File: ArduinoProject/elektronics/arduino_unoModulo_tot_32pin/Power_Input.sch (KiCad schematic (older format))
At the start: 8 parts, among them IC401 MC33269ST-5.OT3, U401 battery, U402 LP2985-3.3

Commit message: sensormodule_x4 added
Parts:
- removed U401: battery, symbol battery
- added X2: DG3XX-02-3.5, degson_DG350-3.5-02P, symbol DG3XX-02-3.5
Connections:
- wire segments 22 -> 20
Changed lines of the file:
@@
 LIBS:MFN_Atmel
 LIBS:MFN_STMicro
+LIBS:degson
 LIBS:Arduino_Uno_R3_From_Scratch-cache
 EELAYER 25 0
@@
 $EndComp
 $Comp
-L battery U401
-U 1 1 5A970BE8
-P 3050 2700
-F 0 "U401" H 3350 1650 60  0000 C CNN
-F 1 "battery" H 2700 2950 60  0000 C CNN
-F 2 "" H 2700 2600 60  0001 C CNN
-F 3 "" H 2700 2600 60  0001 C CNN
-	1    3050 2700
-	1    0    0    -1
-$EndComp
-$Comp
 L D D401
 U 1 1 5A970C82
@@
 Wire Wire Line
 	4450 2800 4850 2800
-Wire Wire Line
-	3000 2300 3900 2300
-Wire Wire Line
-	3900 2300 3900 3900
 $Comp
 L GND #PWR015
 U 1 1 5A970D05
-P 3900 3900
-F 0 "#PWR015" H 3900 3650 50  0001 C CNN
-F 1 "GND" H 3900 3750 50  0000 C CNN
-F 2 "" H 3900 3900 50  0001 C CNN
-F 3 "" H 3900 3900 50  0001 C CNN
-	1    3900 3900
-	1    0    0    -1
-$EndComp
-Wire Wire Line
-	3650 3450 3900 3450
-Connection ~ 3900 3450
+P 3850 2950
+F 0 "#PWR015" H 3850 2700 50  0001 C CNN
+F 1 "GND" H 3850 2800 50  0000 C CNN
+F 2 "" H 3850 2950 50  0001 C CNN
+F 3 "" H 3850 2950 50  0001 C CNN
+	1    3850 2950
+	1    0    0    -1
+$EndComp
 Wire Wire Line
 	4050 2800 4050 2900
@@
 Wire Wire Line
 	7050 2800 5850 2800
-Wire Wire Line
-	6050 2550 6050 3600
 Connection ~ 6050 2800
 Wire Wire Line
@@
 	1    0    0    -1
 $EndComp
+Wire Wire Line
+	6050 2550 6050 3600
+Connection ~ 6050 2900
+Wire Wire Line
+	3650 2950 3850 2950
+$Comp
+L DG3XX-02-3.5 X2
+U 1 1 5AA016CD
+P 3550 2800
+F 0 "X2" H 3670 2765 45  0000 L BNN
+F 1 "DG3XX-02-3.5" H 3550 2800 45  0001 L BNN
+F 2 "degson_DG350-3.5-02P" H 3580 2950 20  0001 C CNN
+F 3 "" H 3550 2800 60  0001 C CNN
+	1    3550 2800
+	-1   0    0    1
+$EndComp
+$Comp
+L DG3XX-02-3.5 X2
+U 2 1 5AA0177C
+P 3550 2950
+F 0 "X2" H 3670 2915 45  0000 L BNN
+F 1 "DG3XX-02-3.5" H 3550 2950 45  0001 L BNN
+F 2 "degson_DG350-3.5-02P" H 3580 3100 20  0001 C CNN
+F 3 "" H 3550 2950 60  0001 C CNN
+	2    3550 2950
+	-1   0    0    1
+$EndComp
 $EndSCHEMATC

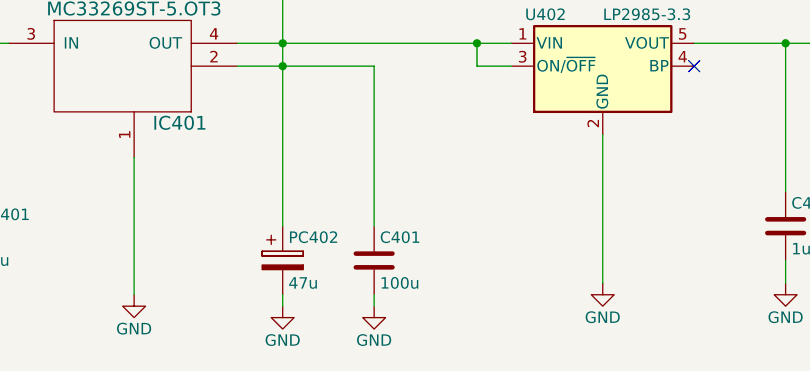
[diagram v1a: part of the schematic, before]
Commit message: arduino routed
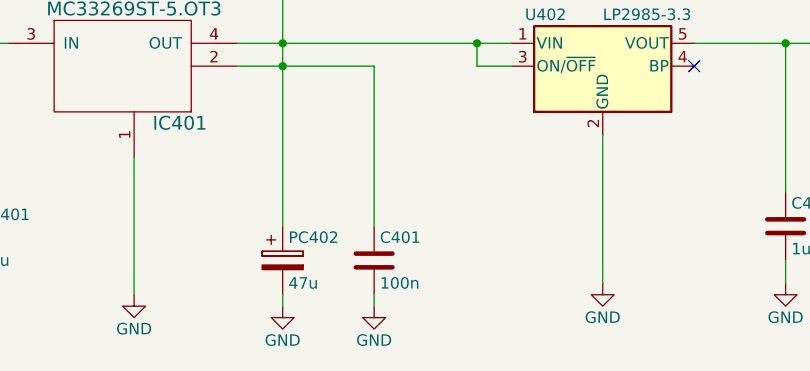
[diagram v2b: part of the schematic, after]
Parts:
- C401: value 100u -> 100n
- IC401: footprint (none) -> MC33269ST-3.3T3G:SOT230P700X175-4N
- X2: footprint degson_DG350-3.5-02P -> degson:degson-DG350-3.5-02P
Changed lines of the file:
@@
 F 0 "IC401" H 5600 2650 60  0000 C CNN
 F 1 "MC33269ST-5.OT3" H 5400 3150 60  0000 C CNN
-F 2 "" H 5050 2800 60  0001 C CNN
+F 2 "MC33269ST-3.3T3G:SOT230P700X175-4N" H 5050 2800 60  0001 C CNN
 F 3 "" H 5050 2800 60  0001 C CNN
 	1    5400 2900
@@
 P 6450 3750
 F 0 "C401" H 6475 3850 50  0000 L CNN
-F 1 "100u" H 6475 3650 50  0000 L CNN
+F 1 "100n" H 6475 3650 50  0000 L CNN
 F 2 "Capacitors_SMD:C_0805" H 6488 3600 50  0001 C CNN
 F 3 "" H 6450 3750 50  0001 C CNN
@@
 F 0 "X2" H 3670 2765 45  0000 L BNN
 F 1 "DG3XX-02-3.5" H 3550 2800 45  0001 L BNN
-F 2 "degson_DG350-3.5-02P" H 3580 2950 20  0001 C CNN
+F 2 "degson:degson-DG350-3.5-02P" H 3580 2950 20  0001 C CNN
 F 3 "" H 3550 2800 60  0001 C CNN
 	1    3550 2800
@@
 F 0 "X2" H 3670 2915 45  0000 L BNN
 F 1 "DG3XX-02-3.5" H 3550 2950 45  0001 L BNN
-F 2 "degson_DG350-3.5-02P" H 3580 3100 20  0001 C CNN
+F 2 "degson:degson-DG350-3.5-02P" H 3580 3100 20  0001 C CNN
 F 3 "" H 3550 2950 60  0001 C CNN
 	2    3550 2950

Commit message: new components2
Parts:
- removed U402: LP2985-3.3, TO_SOT_Packages_SMD:SOT-23-5, symbol LP2985-3.3
- added IC402: MC33269ST-5.OT3, PHT6NQ10T_135:SOT230P700X180-4N, symbol MC33269ST-5.OT3
- D401: footprint Diodes_SMD:D_0805 -> Diodes_SMD:D_MicroMELF_Hadsoldering
- IC401: footprint MC33269ST-3.3T3G:SOT230P700X175-4N -> PHT6NQ10T_135:SOT230P700X180-4N
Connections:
- net +3V3: now also IC402.2, IC402.4 (OUT)
- net +5V: now also IC402.3 (IN)
- net GND: now also IC402.1
- no-connect marks 1 -> 0
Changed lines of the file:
@@
 $EndDescr
-$Comp
-L LP2985-3.3 U402
-U 1 1 5A9664D2
-P 7450 2900
-F 0 "U402" H 7200 3125 50  0000 C CNN
-F 1 "LP2985-3.3" H 7450 3125 50  0000 L CNN
-F 2 "TO_SOT_Packages_SMD:SOT-23-5" H 7450 3225 50  0001 C CNN
-F 3 "" H 7450 2900 50  0001 C CNN
-	1    7450 2900
-	1    0    0    -1
-$EndComp
 $Comp
 L MC33269ST-5.OT3 IC401
@@
 F 0 "IC401" H 5600 2650 60  0000 C CNN
 F 1 "MC33269ST-5.OT3" H 5400 3150 60  0000 C CNN
-F 2 "MC33269ST-3.3T3G:SOT230P700X175-4N" H 5050 2800 60  0001 C CNN
+F 2 "PHT6NQ10T_135:SOT230P700X180-4N" H 5050 2800 60  0001 C CNN
 F 3 "" H 5050 2800 60  0001 C CNN
 	1    5400 2900
@@
 F 0 "D401" H 4300 2900 50  0000 C CNN
 F 1 "D" H 4300 2700 50  0000 C CNN
-F 2 "Diodes_SMD:D_0805" H 4300 2800 50  0001 C CNN
+F 2 "Diodes_SMD:D_MicroMELF_Hadsoldering" H 4300 2800 50  0001 C CNN
 F 3 "" H 4300 2800 50  0001 C CNN
 	1    4300 2800
@@
 Wire Wire Line
 	5400 3900 5400 3300
-Wire Wire Line
-	7050 2800 5850 2800
 Connection ~ 6050 2800
 Wire Wire Line
-	7050 2900 6900 2900
-Wire Wire Line
-	6900 2900 6900 2800
-Connection ~ 6900 2800
-Wire Wire Line
-	7850 2800 8400 2800
+	7700 2800 8400 2800
 Wire Wire Line
 	8250 2800 8250 3450
@@
 L GND #PWR019
 U 1 1 5A97100A
-P 7450 3850
-F 0 "#PWR019" H 7450 3600 50  0001 C CNN
-F 1 "GND" H 7450 3700 50  0000 C CNN
-F 2 "" H 7450 3850 50  0001 C CNN
-F 3 "" H 7450 3850 50  0001 C CNN
-	1    7450 3850
-	1    0    0    -1
-$EndComp
-Wire Wire Line
-	7450 3850 7450 3200
+P 7250 3950
+F 0 "#PWR019" H 7250 3700 50  0001 C CNN
+F 1 "GND" H 7250 3800 50  0000 C CNN
+F 2 "" H 7250 3950 50  0001 C CNN
+F 3 "" H 7250 3950 50  0001 C CNN
+	1    7250 3950
+	1    0    0    -1
+$EndComp
+Wire Wire Line
+	7250 3950 7250 3300
 Wire Wire Line
 	5850 2900 6450 2900
@@
 Wire Wire Line
 	6050 3950 6050 3900
-NoConn ~ 7850 2900
 Connection ~ 8250 2800
 Text HLabel 8400 2800 2    60   Input ~ 0
@@
 	-1   0    0    1
 $EndComp
+$Comp
+L MC33269ST-5.OT3 IC402
+U 1 1 5AA92A2E
+P 7250 2900
+F 0 "IC402" H 7450 2650 60  0000 C CNN
+F 1 "MC33269ST-5.OT3" H 7250 3150 60  0000 C CNN
+F 2 "PHT6NQ10T_135:SOT230P700X180-4N" H 6900 2800 60  0001 C CNN
+F 3 "" H 6900 2800 60  0001 C CNN
+	1    7250 2900
+	1    0    0    -1
+$EndComp
+Wire Wire Line
+	5850 2800 6700 2800
+Wire Wire Line
+	7700 2900 7825 2900
+Wire Wire Line
+	7825 2900 7825 2800
+Connection ~ 7825 2800
 $EndSCHEMATC

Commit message: changes made
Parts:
- D401: footprint Diodes_SMD:D_MicroMELF_Hadsoldering -> Diodes_SMD:D_MiniMELF_Handsoldering
- PC401, PC402: footprint Capacitors_SMD:CP_Elec_4x5.3 -> Capacitors_SMD:CP_Elec_6.3x5.3
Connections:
- net +5V: now also C401.2; no longer C401.1
- net GND: now also C401.1; no longer C401.2
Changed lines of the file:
@@
 F 0 "D401" H 4300 2900 50  0000 C CNN
 F 1 "D" H 4300 2700 50  0000 C CNN
-F 2 "Diodes_SMD:D_MicroMELF_Hadsoldering" H 4300 2800 50  0001 C CNN
+F 2 "Diodes_SMD:D_MiniMELF_Handsoldering" H 4300 2800 50  0001 C CNN
 F 3 "" H 4300 2800 50  0001 C CNN
 	1    4300 2800
 	-1   0    0    1
 $EndComp
-Wire Wire Line
-	3650 2800 4150 2800
-Wire Wire Line
-	4450 2800 4850 2800
 $Comp
 L GND #PWR015
@@
 	1    0    0    -1
 $EndComp
-Wire Wire Line
-	4050 2800 4050 2900
-Connection ~ 4050 2800
 Text HLabel 4050 2900 3    60   Input ~ 0
 PWRIN
-Wire Wire Line
-	4500 2800 4500 2650
-Connection ~ 4500 2800
 Text HLabel 4500 2650 1    60   Input ~ 0
 VIN
-Wire Wire Line
-	4700 2800 4700 3500
-Connection ~ 4700 2800
 $Comp
 L CP PC401
@@
 F 0 "PC401" H 4725 3750 50  0000 L CNN
 F 1 "47u" H 4725 3550 50  0000 L CNN
-F 2 "Capacitors_SMD:CP_Elec_4x5.3" H 4738 3500 50  0001 C CNN
+F 2 "Capacitors_SMD:CP_Elec_6.3x5.3" H 4738 3500 50  0001 C CNN
 F 3 "" H 4700 3650 50  0001 C CNN
 	1    4700 3650
@@
 	1    0    0    -1
 $EndComp
-Wire Wire Line
-	4700 3900 4700 3800
-$Comp
-L GND #PWR017
-U 1 1 5A970E5B
-P 5400 3900
-F 0 "#PWR017" H 5400 3650 50  0001 C CNN
-F 1 "GND" H 5400 3750 50  0000 C CNN
-F 2 "" H 5400 3900 50  0001 C CNN
-F 3 "" H 5400 3900 50  0001 C CNN
-	1    5400 3900
-	1    0    0    -1
-$EndComp
-Wire Wire Line
-	5400 3900 5400 3300
-Connection ~ 6050 2800
-Wire Wire Line
-	7700 2800 8400 2800
-Wire Wire Line
-	8250 2800 8250 3450
 $Comp
 L C C402
@@
 $EndComp
 $Comp
-L GND #PWR018
+L GND #PWR017
 U 1 1 5A970FC8
 P 8250 3850
-F 0 "#PWR018" H 8250 3600 50  0001 C CNN
+F 0 "#PWR017" H 8250 3600 50  0001 C CNN
 F 1 "GND" H 8250 3700 50  0000 C CNN
 F 2 "" H 8250 3850 50  0001 C CNN
@@
 	1    0    0    -1
 $EndComp
-Wire Wire Line
-	8250 3850 8250 3750
-$Comp
-L GND #PWR019
-U 1 1 5A97100A
-P 7250 3950
-F 0 "#PWR019" H 7250 3700 50  0001 C CNN
-F 1 "GND" H 7250 3800 50  0000 C CNN
-F 2 "" H 7250 3950 50  0001 C CNN
-F 3 "" H 7250 3950 50  0001 C CNN
-	1    7250 3950
-	1    0    0    -1
-$EndComp
-Wire Wire Line
-	7250 3950 7250 3300
-Wire Wire Line
-	5850 2900 6450 2900
-Wire Wire Line
-	6450 2900 6450 3600
 $Comp
 L CP PC402
@@
 F 0 "PC402" H 6075 3850 50  0000 L CNN
 F 1 "47u" H 6075 3650 50  0000 L CNN
-F 2 "Capacitors_SMD:CP_Elec_4x5.3" H 6088 3600 50  0001 C CNN
+F 2 "Capacitors_SMD:CP_Elec_6.3x5.3" H 6088 3600 50  0001 C CNN
 F 3 "" H 6050 3750 50  0001 C CNN
 	1    6050 3750
@@
 F 3 "" H 6450 3750 50  0001 C CNN
 	1    6450 3750
-	1    0    0    -1
-$EndComp
-$Comp
-L GND #PWR020
-U 1 1 5A971288
-P 6050 3950
-F 0 "#PWR020" H 6050 3700 50  0001 C CNN
-F 1 "GND" H 6050 3800 50  0000 C CNN
-F 2 "" H 6050 3950 50  0001 C CNN
-F 3 "" H 6050 3950 50  0001 C CNN
-	1    6050 3950
-	1    0    0    -1
-$EndComp
-$Comp
-L GND #PWR021
-U 1 1 5A9712AB
-P 6450 3950
-F 0 "#PWR021" H 6450 3700 50  0001 C CNN
-F 1 "GND" H 6450 3800 50  0000 C CNN
-F 2 "" H 6450 3950 50  0001 C CNN
-F 3 "" H 6450 3950 50  0001 C CNN
-	1    6450 3950
-	1    0    0    -1
-$EndComp
-Wire Wire Line
-	6450 3950 6450 3900
-Wire Wire Line
-	6050 3950 6050 3900
-Connection ~ 8250 2800
+	1    0    0    1
+$EndComp
 Text HLabel 8400 2800 2    60   Input ~ 0
 +3V3
 $Comp
-L +5V #PWR022
+L +5V #PWR018
 U 1 1 5A9E7608
 P 6050 2550
-F 0 "#PWR022" H 6050 2400 50  0001 C CNN
+F 0 "#PWR018" H 6050 2400 50  0001 C CNN
 F 1 "+5V" H 6050 2690 50  0000 C CNN
 F 2 "" H 6050 2550 50  0001 C CNN
@@
 	1    0    0    -1
 $EndComp
-Wire Wire Line
-	6050 2550 6050 3600
-Connection ~ 6050 2900
-Wire Wire Line
-	3650 2950 3850 2950
 $Comp
 L DG3XX-02-3.5 X2
@@
 	1    0    0    -1
 $EndComp
+$Comp
+L GND #PWR019
+U 1 1 5AB2F4BB
+P 6050 3950
+F 0 "#PWR019" H 6050 3700 50  0001 C CNN
+F 1 "GND" H 6050 3800 50  0000 C CNN
+F 2 "" H 6050 3950 50  0001 C CNN
+F 3 "" H 6050 3950 50  0001 C CNN
+	1    6050 3950
+	1    0    0    -1
+$EndComp
+$Comp
+L GND #PWR020
+U 1 1 5A97100A
+P 7250 3950
+F 0 "#PWR020" H 7250 3700 50  0001 C CNN
+F 1 "GND" H 7250 3800 50  0000 C CNN
+F 2 "" H 7250 3950 50  0001 C CNN
+F 3 "" H 7250 3950 50  0001 C CNN
+	1    7250 3950
+	1    0    0    -1
+$EndComp
+$Comp
+L GND #PWR021
+U 1 1 5A970E5B
+P 5400 3900
+F 0 "#PWR021" H 5400 3650 50  0001 C CNN
+F 1 "GND" H 5400 3750 50  0000 C CNN
+F 2 "" H 5400 3900 50  0001 C CNN
+F 3 "" H 5400 3900 50  0001 C CNN
+	1    5400 3900
+	1    0    0    -1
+$EndComp
+$Comp
+L GND #PWR022
+U 1 1 5A9712AB
+P 6450 3950
+F 0 "#PWR022" H 6450 3700 50  0001 C CNN
+F 1 "GND" H 6450 3800 50  0000 C CNN
+F 2 "" H 6450 3950 50  0001 C CNN
+F 3 "" H 6450 3950 50  0001 C CNN
+	1    6450 3950
+	1    0    0    -1
+$EndComp
+Wire Wire Line
+	3650 2800 4150 2800
+Wire Wire Line
+	4450 2800 4850 2800
+Wire Wire Line
+	4050 2800 4050 2900
+Connection ~ 4050 2800
+Wire Wire Line
+	4500 2800 4500 2650
+Connection ~ 4500 2800
+Wire Wire Line
+	4700 2800 4700 3500
+Connection ~ 4700 2800
+Wire Wire Line
+	4700 3900 4700 3800
+Wire Wire Line
+	5400 3900 5400 3300
+Connection ~ 6050 2800
+Wire Wire Line
+	7700 2800 8400 2800
+Wire Wire Line
+	8250 2800 8250 3450
+Wire Wire Line
+	8250 3850 8250 3750
+Wire Wire Line
+	7250 3950 7250 3300
+Wire Wire Line
+	5850 2900 6450 2900
+Wire Wire Line
+	6450 2900 6450 3600
+Connection ~ 8250 2800
+Wire Wire Line
+	6050 2550 6050 3600
+Connection ~ 6050 2900
+Wire Wire Line
+	3650 2950 3850 2950
 Wire Wire Line
 	5850 2800 6700 2800
@@
 	7825 2900 7825 2800
 Connection ~ 7825 2800
+Wire Wire Line
+	6450 3900 6450 3950
+Wire Wire Line
+	6050 3900 6050 3950
 $EndSCHEMATC
